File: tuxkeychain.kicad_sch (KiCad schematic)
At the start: 43 parts, among them J1 Amphenol_10104111, Q2 2N7002, SW1 B3U-1000P, U4 F1C100s, U5 TLV76701DRVx, U6 W25Q128JVS, U7 TLV76701DRVx, U8 TLV76701DRVx, Y1 24MHz

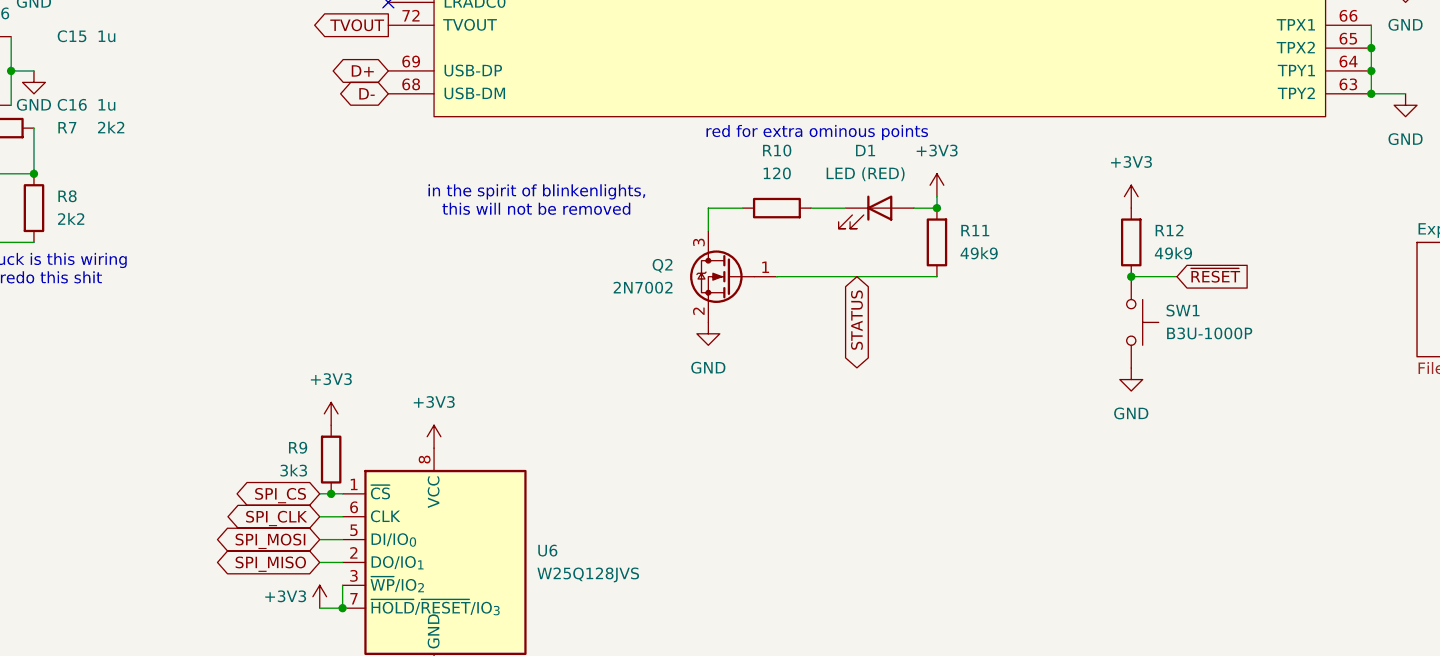
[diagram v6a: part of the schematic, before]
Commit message: change led resistor and add FEL button
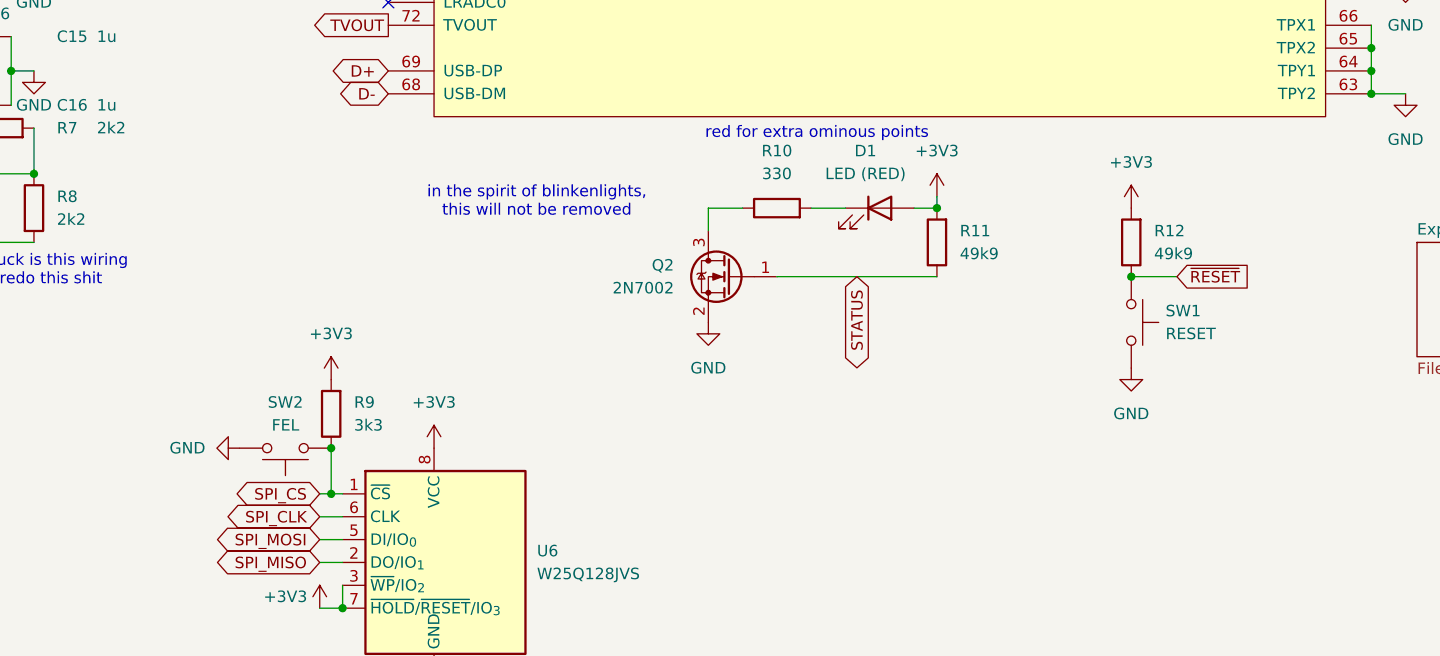
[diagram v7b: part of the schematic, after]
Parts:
- added SW2: FEL, Button_Switch_SMD:SW_SPST_B3U-1000P, symbol Switch:SW_Push
- R10: value 120 -> 330
- SW1: value B3U-1000P -> RESET
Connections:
- net GND: now also SW2.2
- net SPI_CS: now also SW2.1
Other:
- moved on the sheet: R9
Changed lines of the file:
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@@
 	)
 	(junction
+		(at 134.62 165.1)
+		(diameter 0)
+		(color 0 0 0 0)
+	)
+	(junction
 		(at 135.89 182.88)
 		(diameter 0)
@@
 	(wire
 		(pts
+			(xy 134.62 165.1) (xy 134.62 170.18)
+		)
+		(stroke
+			(width 0)
+			(type default)
+		)
+	)
+	(wire
+		(pts
 			(xy 50.8 119.38) (xy 52.07 119.38)
 		)
@@
 	)
 	(symbol
+		(lib_id "Switch:SW_Push")
+		(at 129.54 165.1 180)
+		(unit 1)
+		(exclude_from_sim no)
+		(in_bom yes)
+		(on_board yes)
+		(dnp no)
+		(property "Reference" "SW2"
+			(at 129.54 160.02 0)
+			(effects
+				(font
+					(size 1.27 1.27)
+				)
+			)
+		)
+		(property "Value" "FEL"
+			(at 129.54 162.56 0)
+			(effects
+				(font
+					(size 1.27 1.27)
+				)
+			)
+		)
+		(property "Footprint" "Button_Switch_SMD:SW_SPST_B3U-1000P"
+			(at 129.54 170.18 0)
+			(effects
+				(font
+					(size 1.27 1.27)
+				)
+				(hide yes)
+			)
+		)
+		(property "Datasheet" "~"
+			(at 129.54 170.18 0)
+			(effects
+				(font
+					(size 1.27 1.27)
+				)
+				(hide yes)
+			)
+		)
+		(property "Description" "Push button switch, generic, two pins"
+			(at 129.54 165.1 0)
+			(effects
+				(font
+					(size 1.27 1.27)
+				)
+				(hide yes)
+			)
+		)
+		(pin "2"
+		)
+		(pin "1"
+		)
+		(instances
+			(project "tuxkeychain"
+				(path "/b08030bf-1ef2-4626-81f6-c1cc66f6d9b4"
+					(reference "SW2")
+					(unit 1)
+				)
+			)
+		)
+	)
+	(symbol
 		(lib_id "Device:R")
 		(at 57.15 31.75 90)
@@
 			)
 		)
-		(property "Value" "B3U-1000P"
+		(property "Value" "RESET"
 			(at 227.33 152.3999 90)
 			(effects
@@
 	(symbol
 		(lib_id "Device:R")
-		(at 134.62 166.37 0)
-		(mirror x)
+		(at 134.62 161.29 180)
 		(unit 1)
 		(exclude_from_sim no)
@@
 		(dnp no)
 		(property "Reference" "R9"
-			(at 132.08 165.0999 0)
+			(at 137.16 160.0199 0)
 			(effects
 				(font
@@
 		)
 		(property "Value" "3k3"
-			(at 132.08 167.6399 0)
+			(at 137.16 162.5599 0)
 			(effects
 				(font
@@
 		)
 		(property "Footprint" "Resistor_SMD:R_0402_1005Metric"
-			(at 132.842 166.37 90)
+			(at 136.398 161.29 90)
 			(effects
 				(font
@@
 		)
 		(property "Datasheet" "~"
-			(at 134.62 166.37 0)
+			(at 134.62 161.29 0)
 			(effects
 				(font
@@
 		)
 		(property "Description" "Resistor"
-			(at 134.62 166.37 0)
+			(at 134.62 161.29 0)
 			(effects
 				(font
@@
 	(symbol
 		(lib_id "power:GND")
+		(at 124.46 165.1 270)
+		(unit 1)
+		(exclude_from_sim no)
+		(in_bom yes)
+		(on_board yes)
+		(dnp no)
+		(fields_autoplaced yes)
+		(property "Reference" "#PWR02"
+			(at 118.11 165.1 0)
+			(effects
+				(font
+					(size 1.27 1.27)
+				)
+				(hide yes)
+			)
+		)
+		(property "Value" "GND"
+			(at 120.65 165.0999 90)
+			(effects
+				(font
+					(size 1.27 1.27)
+				)
+				(justify right)
+			)
+		)
+		(property "Footprint" ""
+			(at 124.46 165.1 0)
+			(effects
+				(font
+					(size 1.27 1.27)
+				)
+				(hide yes)
+			)
+		)
+		(property "Datasheet" ""
+			(at 124.46 165.1 0)
+			(effects
+				(font
+					(size 1.27 1.27)
+				)
+				(hide yes)
+			)
+		)
+		(property "Description" "Power symbol creates a global label with name \"GND\" , ground"
+			(at 124.46 165.1 0)
+			(effects
+				(font
+					(size 1.27 1.27)
+				)
+				(hide yes)
+			)
+		)
+		(pin "1"
+		)
+		(instances
+			(project "tuxkeychain"
+				(path "/b08030bf-1ef2-4626-81f6-c1cc66f6d9b4"
+					(reference "#PWR02")
+					(unit 1)
+				)
+			)
+		)
+	)
+	(symbol
+		(lib_id "power:GND")
 		(at 43.18 64.77 0)
 		(unit 1)
@@
 			)
 		)
-		(property "Value" "120"
+		(property "Value" "330"
 			(at 184.15 134.62 90)
 			(effects
@@
 	(symbol
 		(lib_id "power:+3V3")
-		(at 134.62 162.56 0)
+		(at 134.62 157.48 0)
 		(mirror y)
 		(unit 1)
@@
 		(dnp no)
 		(property "Reference" "#PWR024"
-			(at 134.62 166.37 0)
+			(at 134.62 161.29 0)
 			(effects
 				(font
@@
 		)
 		(property "Value" "+3V3"
-			(at 134.62 157.48 0)
+			(at 134.62 152.4 0)
 			(effects
 				(font
@@
 		)
 		(property "Footprint" ""
-			(at 134.62 162.56 0)
+			(at 134.62 157.48 0)
 			(effects
 				(font
@@
 		)
 		(property "Datasheet" ""
-			(at 134.62 162.56 0)
+			(at 134.62 157.48 0)
 			(effects
 				(font
@@
 		)
 		(property "Description" "Power symbol creates a global label with name \"+3V3\""
-			(at 134.62 162.56 0)
+			(at 134.62 157.48 0)
 			(effects
 				(font
